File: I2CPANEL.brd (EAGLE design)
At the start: 100 x 30 mm, 23 parts, among them IC1 MCP23017SO, IC2 128X64 OLED

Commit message: Added second OLED mount
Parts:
- removed JP1: M100.1, freetronics-original:1X10
- removed JP3: OLED, freetronics-jon:1X04
- added FID1, FID2: FIDUCIAL1X2.5, freetronics:FIDUCIAL-1X2.5
- added J1: M10-SOCKET, SuperHouse-Connectors:1X10-S
- added J2: OLED, SuperHouse-Connectors:1X04-P
- added MOD1: OLED-I2C128X64-1.3, SuperHouse-Displays:OLED-128X64-1.3
- C2: device freetronics-master-v1.1:0603 -> SuperHouse-DiscreteSemi:C0603
- IC1: device microchip:SO28W -> SuperHouse-ICs:SO28W
- LED1: device freetronics-jon:LED-0603 -> SuperHouse-LEDs:LED-0603
- R27, R28, R29, R30, R31: device freetronics-master-v1:0603 -> SuperHouse-DiscreteSemi:R0603
- R3: device freetronics-jon:0603 -> SuperHouse-DiscreteSemi:R0603
- S1, S2, S3, S4, S5, S6: device freetronics-original:TACTILE-PTH -> SuperHouse-Switches:TACTILE-PTH-6MM
- moved R29 1.00 mm to (46.0, 26.0)
- moved R30 1.00 mm to (44.0, 26.0)
- moved R31 1.00 mm to (42.0, 26.0)
- moved S1 1.00 mm to (45.0, 15.0)
- moved S2 1.00 mm to (21.0, 15.0)
- moved S3 1.00 mm to (33.0, 22.0)
- moved S4 1.00 mm to (33.0, 8.00)
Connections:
- net GND: now also J1.10, J2.4; no longer JP1.10, JP3.4
- net N$1: now also J1.1; no longer JP1.1
- net N$2: now also J1.2; no longer JP1.2
- net N$3: now also J1.3; no longer JP1.3
- net N$4: now also J1.4; no longer JP1.4
- net N$5: now also J1.5; no longer JP1.5
- net N$7: now also J1.6; no longer JP1.6
- net N$8: now also J1.7; no longer JP1.7
- net N$9: now also J1.8; no longer JP1.8
- net SCL: now also J2.2; no longer JP3.2
- net SDA: now also J2.1; no longer JP3.1
- net VCC: now also J1.9, J2.3; no longer JP1.9, JP3.3
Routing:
- net SDA: track 54.8 -> 53.2 mm
- net SCL: track 52.0 -> 50.5 mm
- net GPA4: track 28.7 -> 27.7 mm
- net GPA3: track 33.7 -> 32.7 mm
- net GPA2: track 49.6 -> 48.6 mm
- net GPA1: track 15.6 -> 14.6 mm
- net ADDR2: track 29.5 -> 28.5 mm
- net ADDR1: track 24.0 -> 23.0 mm
- net ADDR0: track 18.2 -> 17.2 mm
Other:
- board text added: "I2C Pullups"
- board text added: "VCC"
- board text added: "v2.0"
- board text removed: "I2C P/U"
- board text removed: "v1.0"

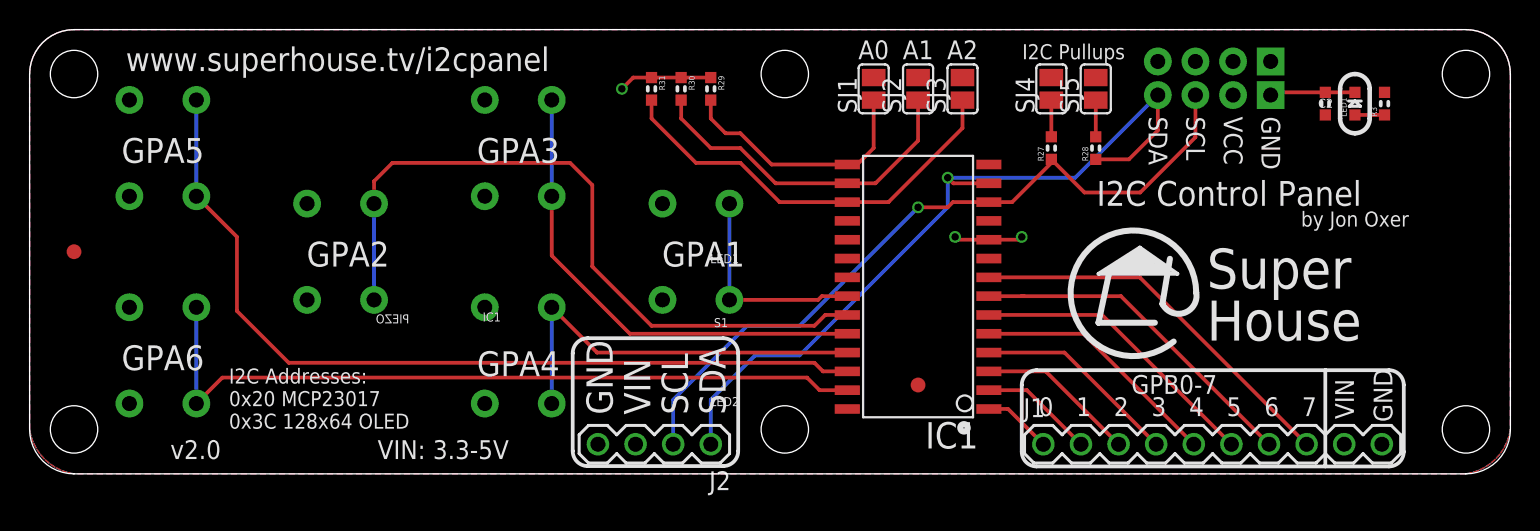
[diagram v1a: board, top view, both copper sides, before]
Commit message: Renumbered designators to simplify BOM
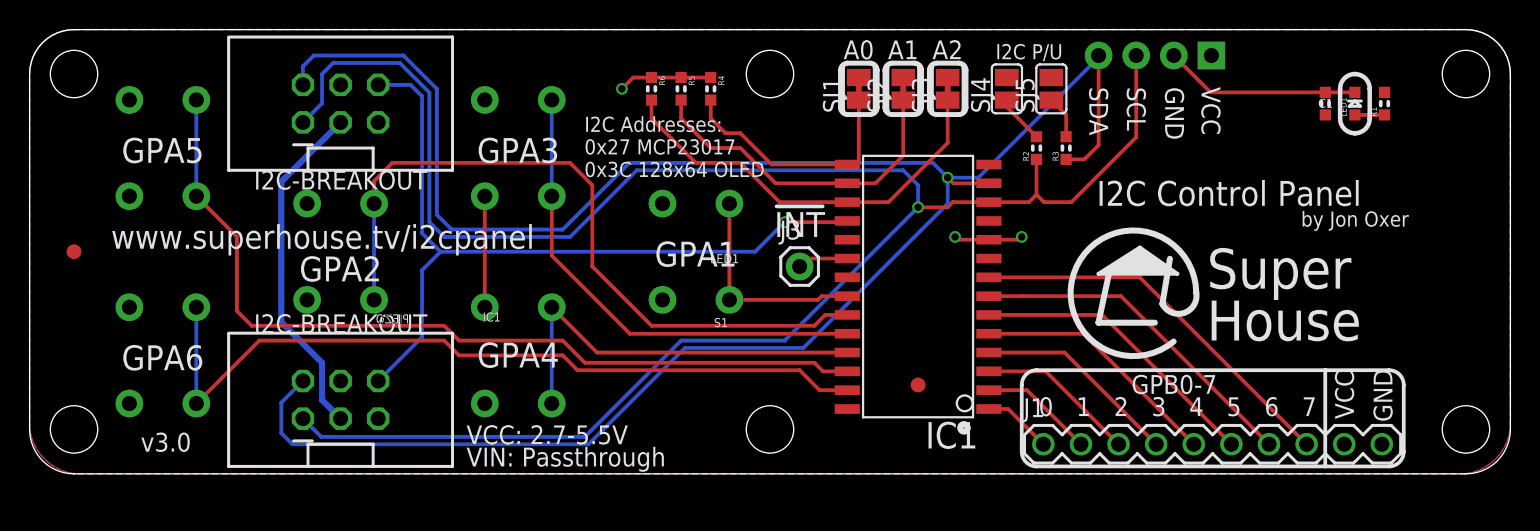
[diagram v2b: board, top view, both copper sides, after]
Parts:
- removed IC2: 128X64 OLED, freetronics-jon:OLED-128X64
- removed R27, R28: 4K7, SuperHouse-DiscreteSemi:R0603
- added J3: M01-PLAIN, SuperHouse-Connectors:1X01
- added J4: I2C-BREAKOUT, SuperHouse-Connectors:2X03-SHROUDED
- added R1, R2: 4K7, SuperHouse-DiscreteSemi:R0603
- J2: value OLED -> I2C-BREAKOUT; device SuperHouse-Connectors:1X04-P -> SuperHouse-Connectors:2X03-SHROUDED
- SJ1, SJ2, SJ3: value (none) -> SJC; device freetronics-jon:SJ -> SuperHouse-Jumpers:SJC
- moved J2 34.0 mm to (21.0, 25.0), turned to 90 degrees
- moved R3 21.7 mm to (70.0, 22.0)
- moved MOD1 4.02 mm to (76.0, 13.5)
- moved SJ4 3.00 mm to (66.0, 26.0)
- moved SJ5 3.00 mm to (69.0, 26.0)
- moved SJ1 1.00 mm to (56.0, 26.0)
- moved SJ2 1.00 mm to (59.0, 26.0)
- moved SJ3 1.00 mm to (62.0, 26.0)
- renumbered C2 to C1, R29 to R4, R30 to R5, R31 to R6
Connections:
- new net !INT: IC1.20, J3.1
- new net !RESET: IC1.18, J2.6, J4.6
- new net VIN: J2.3, J4.3
- net GND: now also J4.4, MOD1.GND; no longer IC2.GND
- net N$42: now also R2.2; no longer R27.2
- net N$43: now also R3.2; no longer R28.2
- net N$6: now also R1.1; no longer R3.1
- net SCL: now also J2.1, J4.1, MOD1.SCL, R2.1; no longer IC2.SCL, J2.2, R27.1
- net SDA: now also J2.2, J4.2, MOD1.SDA, R3.1; no longer IC2.SDA, J2.1, R28.1
- net VCC: now also J2.5, J4.5, MOD1.VCC, R1.2; no longer IC1.18, IC2.VCC, J2.3, R3.2
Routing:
- net SDA: track 53.2 -> 140.4 mm
- net SCL: track 50.5 -> 131.6 mm
- net !RESET: track 0.00 -> 53.1 mm, vias 0 -> 1
- net VIN: track 0.00 -> 23.3 mm
- net GND: track 16.7 -> 31.7 mm
- net !INT: track 0.00 -> 3.44 mm
- net GPA6: track 51.5 -> 53.6 mm
- net N$42: track 2.48 -> 3.30 mm
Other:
- board text added: "!INT"
- board text added: "!RST"
- board text added: "Copyright 2019-2020 SuperHouse Automation Pty Ltd Released under the TAPR Open Hardware License www.tapr.org/OHL"
- board text added: "I2C Addresses: 0x27 MCP23017 0x3C 128x64 OLED"
- board text added: "I2C P/U"
- board text added: "I2C-BREAKOUT"
- board text added: "VCC: 2.7-5.5V"
- board text added: "VIN: Passthrough"
- board text added: "v3.0"
- board text removed: "Copyright 2019 SuperHouse Automation Pty Ltd Released under the TAPR Open Hardware License www.tapr.org/OHL"
- board text removed: "I2C Addresses: 0x20 MCP23017 0x3C 128x64 OLED"
- board text removed: "I2C Pullups"
- board text removed: "LED2"
- board text removed: "VIN: 3.3-5V"
- board text removed: "v2.0"
